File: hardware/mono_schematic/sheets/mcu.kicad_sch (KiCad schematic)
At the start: 26 parts, among them SW1 KMR2, U1 ESP32-S3FN8, Y1 L327S400H11L

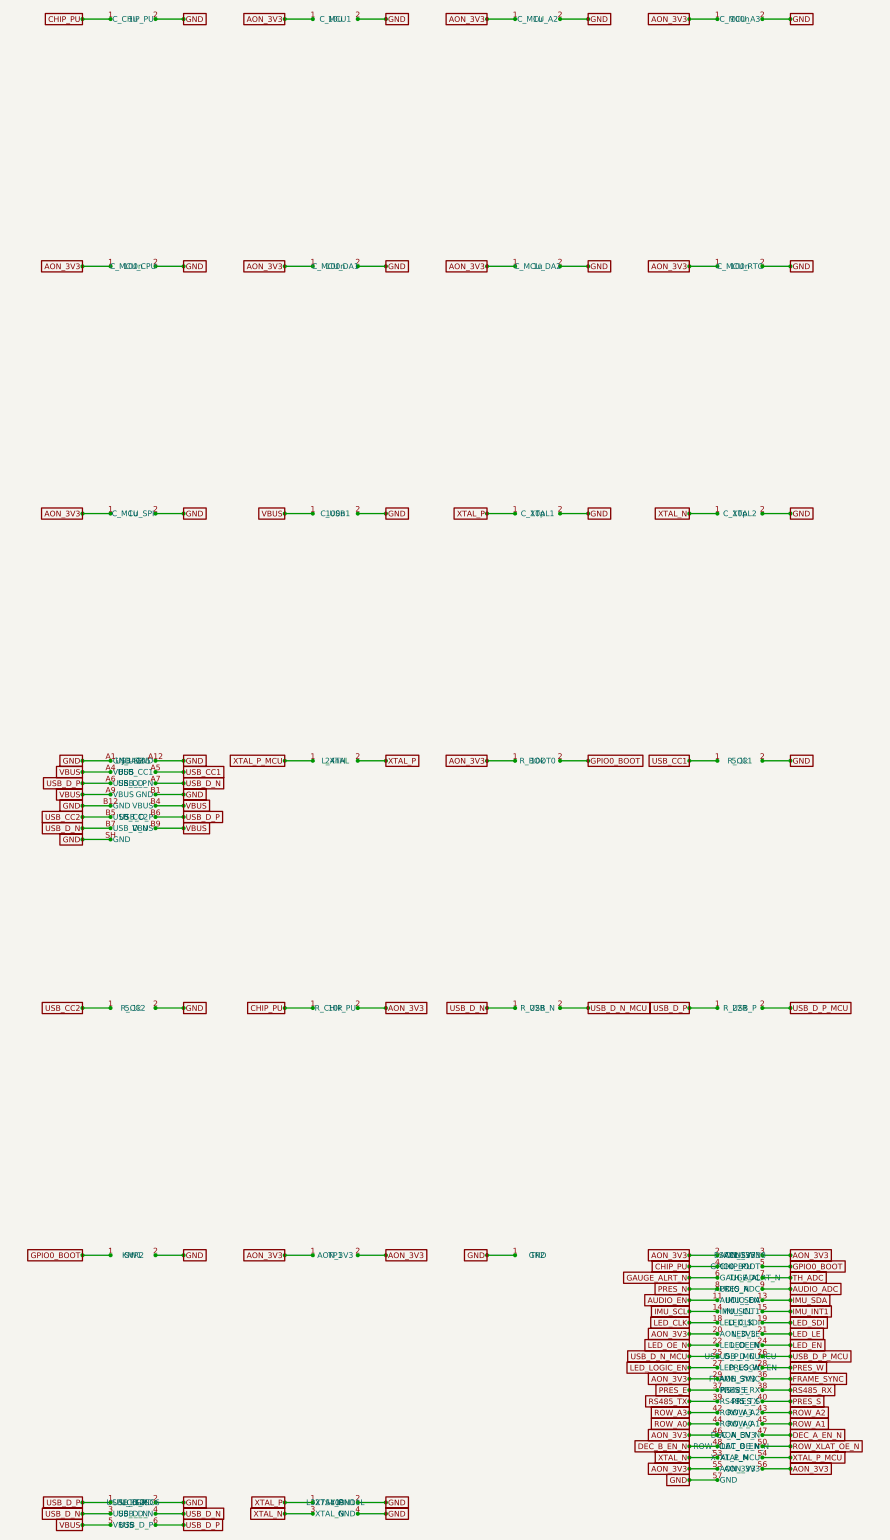
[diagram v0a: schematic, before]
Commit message: mono_electronics v11b: TLV75733P 1A AON LDO, 22uF ESP32 bulk, LED_EN RC glitch filter, J_USB value, refs end in digit; schematic regenerated (ERC 0, 0 diffs)
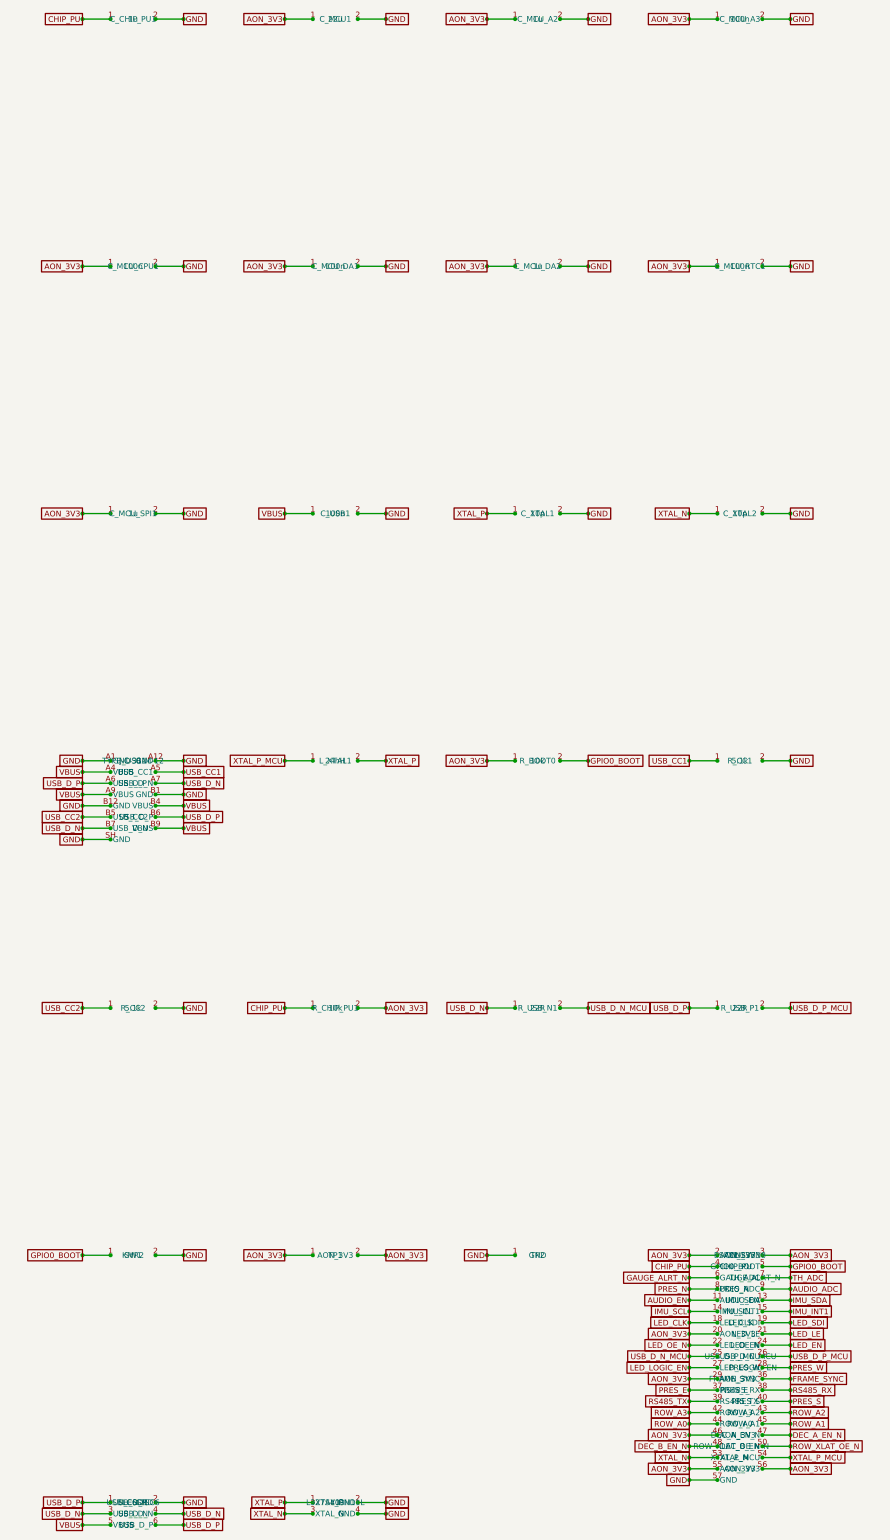
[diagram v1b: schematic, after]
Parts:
- removed C_CHIP_PU, C_MCU_SPI: 1u, mono_electronics:C_0402_1005Metric, symbol mono_parts:1u_C_0402_1005Metric_2
- removed C_MCU1: 10u, mono_electronics:C_0805_2012Metric, symbol mono_parts:10u_C_0805_2012Metric_2
- removed C_MCU_CPU, C_MCU_RTC: 100n, mono_electronics:C_0402_1005Metric, symbol mono_parts:100n_C_0402_1005Metric_2
- removed J_USB: USB4105, mono_electronics:USB_C_Receptacle_HRO_TYPE-C-31-M-12, symbol mono_parts:USB4105_USB_C_Receptacle_HRO_TYPE-C-31-M-12_15
- removed L_XTAL: 24nH, mono_electronics:L_0402_1005Metric, symbol mono_parts:24nH_L_0402_1005Metric_2
- removed R_CHIP_PU: 10k, mono_electronics:R_0402_1005Metric, symbol mono_parts:10k_R_0402_1005Metric_2
- removed R_USB_N, R_USB_P: 22R, mono_electronics:R_0402_1005Metric, symbol mono_parts:22R_R_0402_1005Metric_2
- removed U_ESD: USBLC6-2SC6, mono_electronics:SOT-23-6, symbol mono_parts:USBLC6-2SC6_SOT-23-6_6
- added C_CHIP_PU1, C_MCU_SPI1: 1u, mono_electronics:C_0402_1005Metric, symbol mono_parts:1u_C_0402_1005Metric_2
- added C_MCU1: 22u, mono_electronics:C_0805_2012Metric, symbol mono_parts:22u_C_0805_2012Metric_2
- added C_MCU_CPU1, C_MCU_RTC1: 100n, mono_electronics:C_0402_1005Metric, symbol mono_parts:100n_C_0402_1005Metric_2
- added J_USB1: TYPE-C-31-M-12, mono_electronics:USB_C_Receptacle_HRO_TYPE-C-31-M-12, symbol mono_parts:TYPE-C-31-M-12_USB_C_Receptacle_HRO_TYPE-C-31-M-12_15
- added L_XTAL1: 24nH, mono_electronics:L_0402_1005Metric, symbol mono_parts:24nH_L_0402_1005Metric_2
- added R_CHIP_PU1: 10k, mono_electronics:R_0402_1005Metric, symbol mono_parts:10k_R_0402_1005Metric_2
- added R_USB_N1, R_USB_P1: 22R, mono_electronics:R_0402_1005Metric, symbol mono_parts:22R_R_0402_1005Metric_2
- added U_ESD1: USBLC6-2SC6, mono_electronics:SOT-23-6, symbol mono_parts:USBLC6-2SC6_SOT-23-6_6
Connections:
- net AON_3V3: now also C_MCU1.1, C_MCU_CPU1.1, C_MCU_RTC1.1, C_MCU_SPI1.1, R_CHIP_PU1.2
- net CHIP_PU: now also C_CHIP_PU1.1, R_CHIP_PU1.1
- net GND: now also C_CHIP_PU1.2, C_MCU1.2, C_MCU_CPU1.2, C_MCU_RTC1.2, C_MCU_SPI1.2, J_USB1.A1 (GND), J_USB1.A12 (GND), J_USB1.B1 (GND), J_USB1.B12 (GND), J_USB1.SH (GND), U_ESD1.2 (GND)
- net USB_CC1: now also J_USB1.A5 (USB_CC1)
- net USB_CC2: now also J_USB1.B5 (USB_CC2)
- net USB_D_N: now also J_USB1.A7 (USB_D_N), J_USB1.B7 (USB_D_N), R_USB_N1.1, U_ESD1.3 (USB_D_N), U_ESD1.4 (USB_D_N)
- net USB_D_N_MCU: now also R_USB_N1.2
- net USB_D_P: now also J_USB1.A6 (USB_D_P), J_USB1.B6 (USB_D_P), R_USB_P1.1, U_ESD1.1 (USB_D_P), U_ESD1.6 (USB_D_P)
- net USB_D_P_MCU: now also R_USB_P1.2
- net VBUS: now also J_USB1.A4 (VBUS), J_USB1.A9 (VBUS), J_USB1.B4 (VBUS), J_USB1.B9 (VBUS), U_ESD1.5 (VBUS)
- net XTAL_P: now also L_XTAL1.2
- net XTAL_P_MCU: now also L_XTAL1.1
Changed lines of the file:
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@@
     (property
       "Reference"
-      "C_CHIP_PU"
+      "C_CHIP_PU1"
       (at 35.56 35.56 0)
       (effects
@@
     (instances
       (project "mono_electronics"
-        (path "/d095d7a2-32cb-4d63-9fb9-6767b52b7dfb"
-          (reference "C_CHIP_PU")
+        (path "/ebb28527-3233-4a2a-8697-1d72b07aa22c"
+          (reference "C_CHIP_PU1")
           (unit 1)
         )
@@
   )
   (symbol
-    (lib_id "mono_parts:10u_C_0805_2012Metric_2")
+    (lib_id "mono_parts:22u_C_0805_2012Metric_2")
     (at 81.28 35.56 0)
     (unit 1)
@@
     (property
       "Value"
-      "10u"
+      "22u"
       (at 81.28 35.56 0)
       (effects
@@
     (instances
       (project "mono_electronics"
-        (path "/d095d7a2-32cb-4d63-9fb9-6767b52b7dfb"
+        (path "/ebb28527-3233-4a2a-8697-1d72b07aa22c"
           (reference "C_MCU1")
           (unit 1)
@@
     (instances
       (project "mono_electronics"
-        (path "/d095d7a2-32cb-4d63-9fb9-6767b52b7dfb"
+        (path "/ebb28527-3233-4a2a-8697-1d72b07aa22c"
           (reference "C_MCU_A2")
           (unit 1)
@@
     (instances
       (project "mono_electronics"
-        (path "/d095d7a2-32cb-4d63-9fb9-6767b52b7dfb"
+        (path "/ebb28527-3233-4a2a-8697-1d72b07aa22c"
           (reference "C_MCU_A3")
           (unit 1)
@@
     (property
       "Reference"
-      "C_MCU_CPU"
+      "C_MCU_CPU1"
       (at 35.56 91.44 0)
       (effects
@@
     (instances
       (project "mono_electronics"
-        (path "/d095d7a2-32cb-4d63-9fb9-6767b52b7dfb"
-          (reference "C_MCU_CPU")
+        (path "/ebb28527-3233-4a2a-8697-1d72b07aa22c"
+          (reference "C_MCU_CPU1")
           (unit 1)
         )
@@
     (instances
       (project "mono_electronics"
-        (path "/d095d7a2-32cb-4d63-9fb9-6767b52b7dfb"
+        (path "/ebb28527-3233-4a2a-8697-1d72b07aa22c"
           (reference "C_MCU_DA1")
           (unit 1)
@@
     (instances
       (project "mono_electronics"
-        (path "/d095d7a2-32cb-4d63-9fb9-6767b52b7dfb"
+        (path "/ebb28527-3233-4a2a-8697-1d72b07aa22c"
           (reference "C_MCU_DA2")
           (unit 1)
@@
     (property
       "Reference"
-      "C_MCU_RTC"
+      "C_MCU_RTC1"
       (at 172.72 91.44 0)
       (effects
@@
     (instances
       (project "mono_electronics"
-        (path "/d095d7a2-32cb-4d63-9fb9-6767b52b7dfb"
-          (reference "C_MCU_RTC")
+        (path "/ebb28527-3233-4a2a-8697-1d72b07aa22c"
+          (reference "C_MCU_RTC1")
           (unit 1)
         )
@@
     (property
       "Reference"
-      "C_MCU_SPI"
+      "C_MCU_SPI1"
       (at 35.56 147.32 0)
       (effects
@@
     (instances
       (project "mono_electronics"
-        (path "/d095d7a2-32cb-4d63-9fb9-6767b52b7dfb"
-          (reference "C_MCU_SPI")
+        (path "/ebb28527-3233-4a2a-8697-1d72b07aa22c"
+          (reference "C_MCU_SPI1")
           (unit 1)
         )
@@
     (instances
       (project "mono_electronics"
-        (path "/d095d7a2-32cb-4d63-9fb9-6767b52b7dfb"
+        (path "/ebb28527-3233-4a2a-8697-1d72b07aa22c"
           (reference "C_USB1")
           (unit 1)
@@
     (instances
       (project "mono_electronics"
-        (path "/d095d7a2-32cb-4d63-9fb9-6767b52b7dfb"
+        (path "/ebb28527-3233-4a2a-8697-1d72b07aa22c"
           (reference "C_XTAL1")
           (unit 1)
@@
     (instances
       (project "mono_electronics"
-        (path "/d095d7a2-32cb-4d63-9fb9-6767b52b7dfb"
+        (path "/ebb28527-3233-4a2a-8697-1d72b07aa22c"
           (reference "C_XTAL2")
           (unit 1)
@@
   )
   (symbol
-    (lib_id "mono_parts:USB4105_USB_C_Receptacle_HRO_TYPE-C-31-M-12_15")
+    (lib_id "mono_parts:TYPE-C-31-M-12_USB_C_Receptacle_HRO_TYPE-C-31-M-12_15")
     (at 35.56 203.2 0)
     (unit 1)
@@
     (property
       "Reference"
-      "J_USB"
+      "J_USB1"
       (at 35.56 203.2 0)
       (effects
@@
     (property
       "Value"
-      "USB4105"
+      "TYPE-C-31-M-12"
       (at 35.56 203.2 0)
       (effects
@@
     (instances
       (project "mono_electronics"
-        (path "/d095d7a2-32cb-4d63-9fb9-6767b52b7dfb"
-          (reference "J_USB")
+        (path "/ebb28527-3233-4a2a-8697-1d72b07aa22c"
+          (reference "J_USB1")
           (unit 1)
         )
@@
     (property
       "Reference"
-      "L_XTAL"
+      "L_XTAL1"
       (at 81.28 203.2 0)
       (effects
@@
     (instances
       (project "mono_electronics"
-        (path "/d095d7a2-32cb-4d63-9fb9-6767b52b7dfb"
-          (reference "L_XTAL")
+        (path "/ebb28527-3233-4a2a-8697-1d72b07aa22c"
+          (reference "L_XTAL1")
           (unit 1)
         )
@@
     (instances
       (project "mono_electronics"
-        (path "/d095d7a2-32cb-4d63-9fb9-6767b52b7dfb"
+        (path "/ebb28527-3233-4a2a-8697-1d72b07aa22c"
           (reference "R_BOOT0")
           (unit 1)
@@
     (instances
       (project "mono_electronics"
-        (path "/d095d7a2-32cb-4d63-9fb9-6767b52b7dfb"
+        (path "/ebb28527-3233-4a2a-8697-1d72b07aa22c"
           (reference "R_CC1")
           (unit 1)
@@
     (instances
       (project "mono_electronics"
-        (path "/d095d7a2-32cb-4d63-9fb9-6767b52b7dfb"
+        (path "/ebb28527-3233-4a2a-8697-1d72b07aa22c"
           (reference "R_CC2")
           (unit 1)
@@
     (property
       "Reference"
-      "R_CHIP_PU"
+      "R_CHIP_PU1"
       (at 81.28 259.08 0)
       (effects
@@
     (instances
       (project "mono_electronics"
-        (path "/d095d7a2-32cb-4d63-9fb9-6767b52b7dfb"
-          (reference "R_CHIP_PU")
+        (path "/ebb28527-3233-4a2a-8697-1d72b07aa22c"
+          (reference "R_CHIP_PU1")
           (unit 1)
         )
@@
     (property
       "Reference"
-      "R_USB_N"
+      "R_USB_N1"
       (at 127 259.08 0)
       (effects
@@
     (instances
       (project "mono_electronics"
-        (path "/d095d7a2-32cb-4d63-9fb9-6767b52b7dfb"
-          (reference "R_USB_N")
+        (path "/ebb28527-3233-4a2a-8697-1d72b07aa22c"
+          (reference "R_USB_N1")
           (unit 1)
         )
@@
     (property
       "Reference"
-      "R_USB_P"
+      "R_USB_P1"
       (at 172.72 259.08 0)
       (effects
@@
     (instances
       (project "mono_electronics"
-        (path "/d095d7a2-32cb-4d63-9fb9-6767b52b7dfb"
-          (reference "R_USB_P")
+        (path "/ebb28527-3233-4a2a-8697-1d72b07aa22c"
+          (reference "R_USB_P1")
           (unit 1)
         )
@@
     (instances
       (project "mono_electronics"
-        (path "/d095d7a2-32cb-4d63-9fb9-6767b52b7dfb"
+        (path "/ebb28527-3233-4a2a-8697-1d72b07aa22c"
           (reference "SW1")
           (unit 1)
@@
     (instances
       (project "mono_electronics"
-        (path "/d095d7a2-32cb-4d63-9fb9-6767b52b7dfb"
+        (path "/ebb28527-3233-4a2a-8697-1d72b07aa22c"
           (reference "TP1")
           (unit 1)
@@
     (instances
       (project "mono_electronics"
-        (path "/d095d7a2-32cb-4d63-9fb9-6767b52b7dfb"
+        (path "/ebb28527-3233-4a2a-8697-1d72b07aa22c"
           (reference "TP2")
           (unit 1)
@@
     (instances
       (project "mono_electronics"
-        (path "/d095d7a2-32cb-4d63-9fb9-6767b52b7dfb"
+        (path "/ebb28527-3233-4a2a-8697-1d72b07aa22c"
           (reference "U1")
           (unit 1)
@@
     (property
       "Reference"
-      "U_ESD"
+      "U_ESD1"
       (at 35.56 370.84 0)
       (effects
@@
     (instances
       (project "mono_electronics"
-        (path "/d095d7a2-32cb-4d63-9fb9-6767b52b7dfb"
-          (reference "U_ESD")
+        (path "/ebb28527-3233-4a2a-8697-1d72b07aa22c"
+          (reference "U_ESD1")
           (unit 1)
         )
@@
     (instances
       (project "mono_electronics"
-        (path "/d095d7a2-32cb-4d63-9fb9-6767b52b7dfb"
+        (path "/ebb28527-3233-4a2a-8697-1d72b07aa22c"
           (reference "Y1")
           (unit 1)
@@
   )
   (sheet_instances
-    (path "/d095d7a2-32cb-4d63-9fb9-6767b52b7dfb"
+    (path "/ebb28527-3233-4a2a-8697-1d72b07aa22c"
       (page "1")
     )
